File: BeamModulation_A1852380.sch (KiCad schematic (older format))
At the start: 0 parts

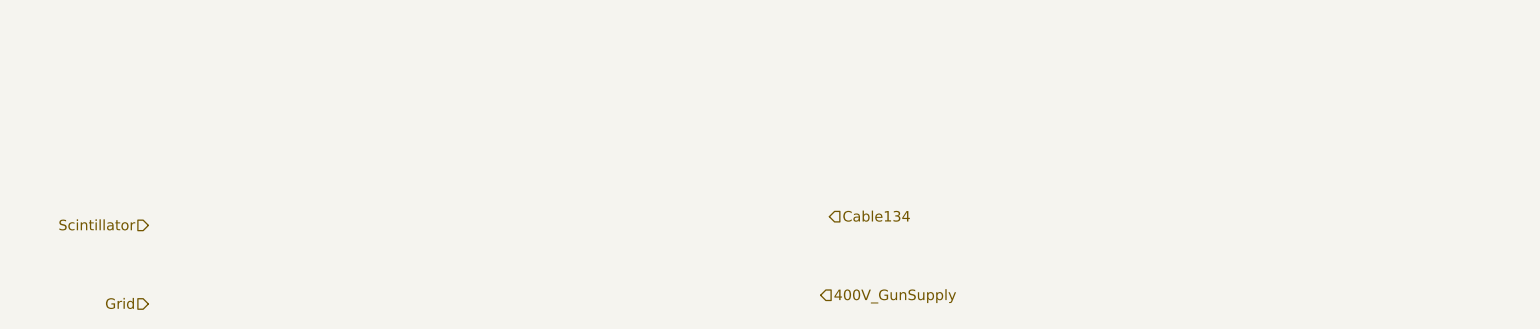
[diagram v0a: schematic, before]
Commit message: Adds Beam Modulation PCB
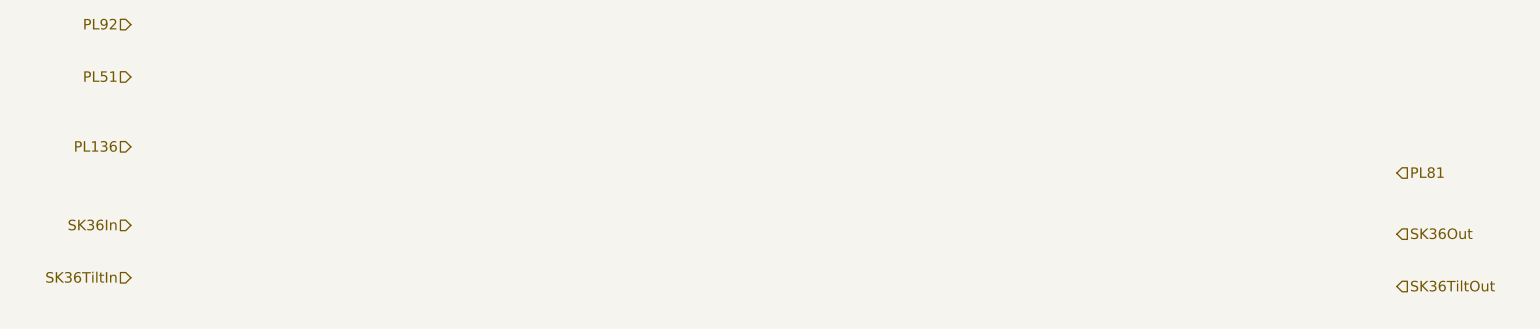
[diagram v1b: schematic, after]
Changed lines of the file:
@@
 $Descr A4 11693 8268
 encoding utf-8
-Sheet 15 19
+Sheet 19 19
 Title ""
 Date ""
@@
 Comment4 ""
 $EndDescr
-Text HLabel 2050 2400 0    60   Input ~ 0
-Scintillator
-Text HLabel 2050 2850 0    60   Input ~ 0
-Grid
-Text HLabel 5950 2350 2    60   Input ~ 0
-Cable134
-Text HLabel 5900 2800 2    60   Input ~ 0
-400V_GunSupply
+Text HLabel 1950 1550 0    60   Input ~ 0
+PL51
+Text HLabel 1950 1250 0    60   Input ~ 0
+PL92
+Text HLabel 1950 2400 0    60   Input ~ 0
+SK36In
+Text HLabel 1950 2700 0    60   Input ~ 0
+SK36TiltIn
+Text HLabel 9200 2450 2    60   Input ~ 0
+SK36Out
+Text HLabel 9200 2750 2    60   Input ~ 0
+SK36TiltOut
+Text HLabel 9200 2100 2    60   Input ~ 0
+PL81
+Text HLabel 1950 1950 0    60   Input ~ 0
+PL136
 $EndSCHEMATC
